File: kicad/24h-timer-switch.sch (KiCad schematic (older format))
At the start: 13 parts, among them J1 Barrel_Jack, J2 Screw_Terminal_01x02, Q1 AO4620, SW1 SW_SPST, U1 AMS1117-5.0, U2 ATtiny85-20PU

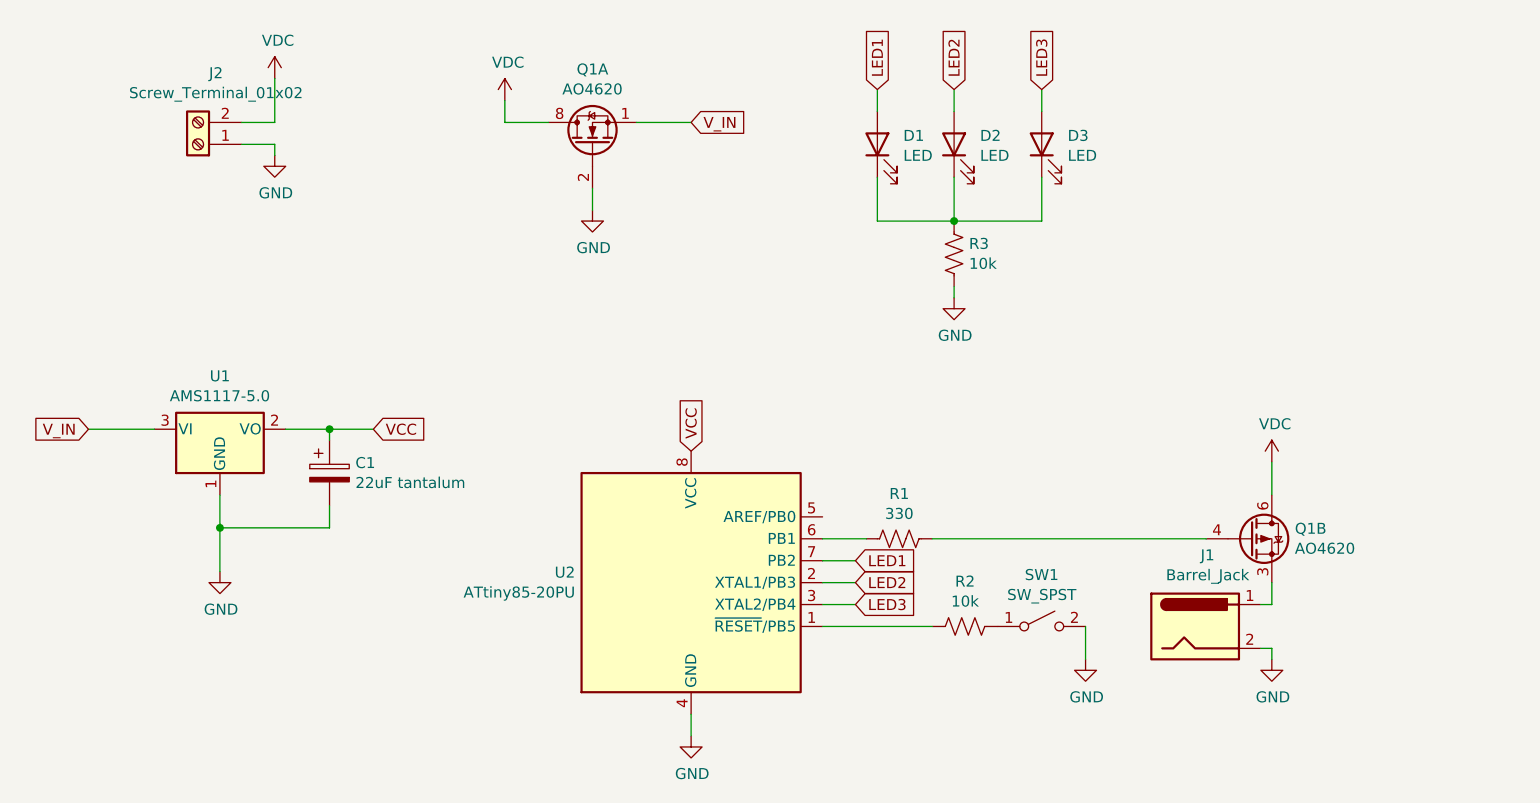
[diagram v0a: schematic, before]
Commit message: add jumper selector
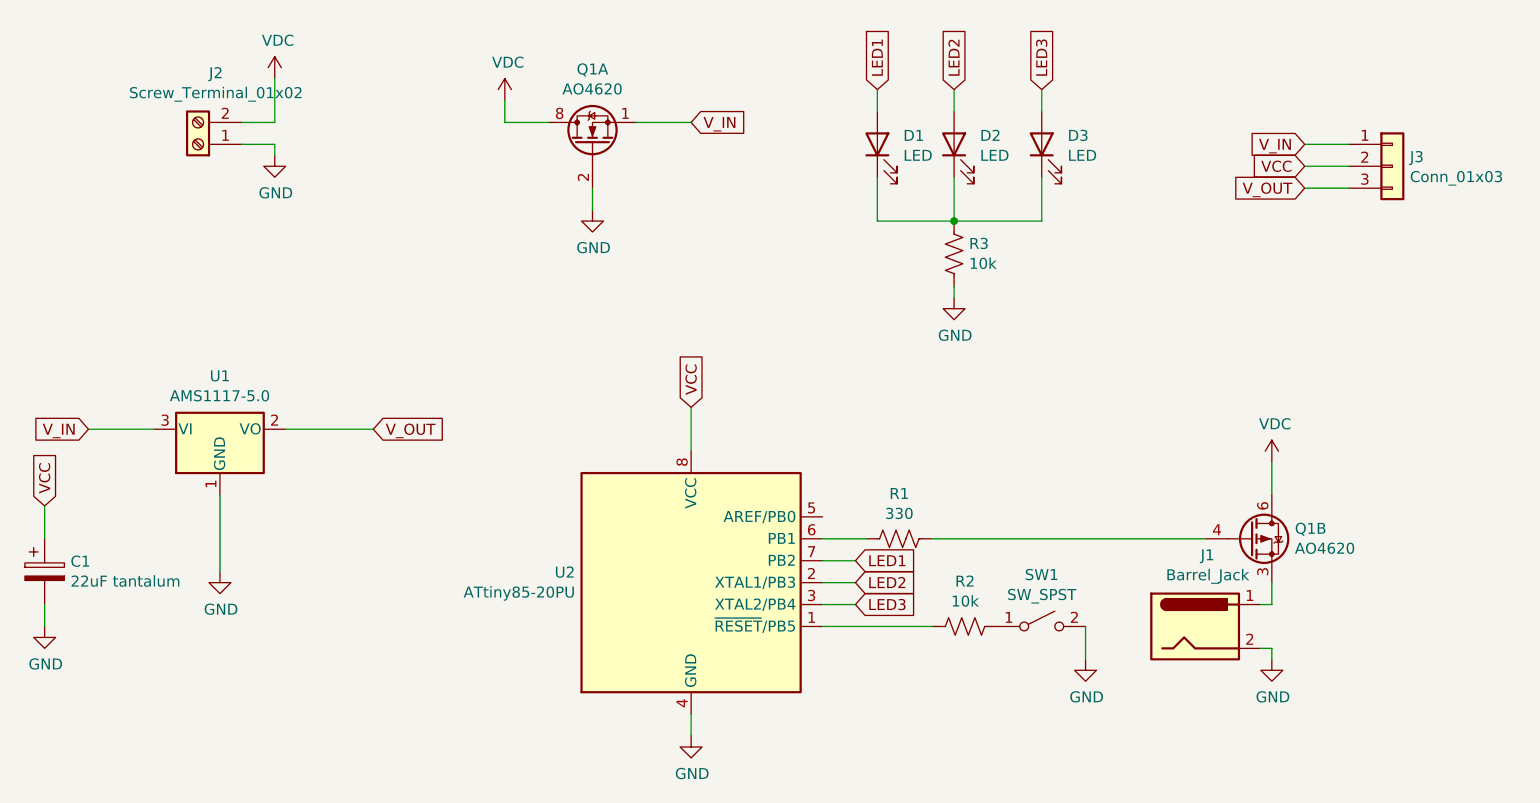
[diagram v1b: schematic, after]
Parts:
- added J3: Conn_01x03, Connector_PinSocket_2.54mm:PinSocket_1x03_P2.54mm_Vertical, symbol Connector_Generic:Conn_01x03
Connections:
- net VCC: now also J3.2 (Pin_2); no longer U1.2 (VO)
- net V_IN: now also J3.1 (Pin_1)
- new net V_OUT: J3.3 (Pin_3), U1.2 (VO)
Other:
- moved on the sheet: C1
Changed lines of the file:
@@
 	1    0    0    -1
 $EndComp
-Wire Wire Line
-	2200 2950 2200 3100
 $Comp
 L Device:CP C1
 U 1 1 61A472D0
-P 2700 2850
-F 0 "C1" H 2818 2896 50  0000 L CNN
-F 1 "22uF tantalum" H 2818 2805 50  0000 L CNN
-F 2 "Capacitor_THT:CP_Radial_D5.0mm_P2.50mm" H 2738 2700 50  0001 C CNN
-F 3 "~" H 2700 2850 50  0001 C CNN
-	1    2700 2850
-	1    0    0    -1
-$EndComp
-Wire Wire Line
-	2500 2650 2700 2650
-Wire Wire Line
-	2700 2650 2700 2700
-Wire Wire Line
-	2700 3000 2700 3100
-Wire Wire Line
-	2700 3100 2200 3100
-Wire Wire Line
-	2200 3100 2200 3300
-Connection ~ 2200 3100
+P 1400 3300
+F 0 "C1" H 1518 3346 50  0000 L CNN
+F 1 "22uF tantalum" H 1518 3255 50  0000 L CNN
+F 2 "Capacitor_THT:CP_Radial_D5.0mm_P2.50mm" H 1438 3150 50  0001 C CNN
+F 3 "~" H 1400 3300 50  0001 C CNN
+	1    1400 3300
+	1    0    0    -1
+$EndComp
 $Comp
 L power:VDC #PWR02
@@
 	1    0    0    -1
 $EndComp
-Wire Wire Line
-	2700 2650 2900 2650
-Connection ~ 2700 2650
 Text GLabel 2900 2650 2    50   Input ~ 0
-VCC
-Text GLabel 4350 2750 1    50   Input ~ 0
-VCC
+V_OUT
+Text GLabel 7150 1550 0    50   Input ~ 0
+V_OUT
 $Comp
 L Device:R_US R1
@@
 Wire Wire Line
 	7000 3650 6950 3650
+$Comp
+L Connector_Generic:Conn_01x03 J3
+U 1 1 61A4A1CB
+P 7550 1450
+F 0 "J3" H 7630 1492 50  0000 L CNN
+F 1 "Conn_01x03" H 7630 1401 50  0000 L CNN
+F 2 "Connector_PinSocket_2.54mm:PinSocket_1x03_P2.54mm_Vertical" H 7550 1450 50  0001 C CNN
+F 3 "~" H 7550 1450 50  0001 C CNN
+	1    7550 1450
+	1    0    0    -1
+$EndComp
+Wire Wire Line
+	7150 1550 7350 1550
+Text GLabel 7150 1350 0    50   Input ~ 0
+V_IN
+Wire Wire Line
+	7150 1350 7350 1350
+Text GLabel 4350 2550 1    50   Input ~ 0
+VCC
+Wire Wire Line
+	4350 2550 4350 2750
+Text GLabel 7150 1450 0    50   Input ~ 0
+VCC
+Wire Wire Line
+	7150 1450 7350 1450
+Wire Wire Line
+	2200 2950 2200 3300
+Wire Wire Line
+	2900 2650 2500 2650
+$Comp
+L power:GND #PWR?
+U 1 1 61A6F596
+P 1400 3550
+F 0 "#PWR?" H 1400 3300 50  0001 C CNN
+F 1 "GND" H 1405 3377 50  0000 C CNN
+F 2 "" H 1400 3550 50  0001 C CNN
+F 3 "" H 1400 3550 50  0001 C CNN
+	1    1400 3550
+	1    0    0    -1
+$EndComp
+Wire Wire Line
+	1400 3450 1400 3550
+Text GLabel 1400 3000 1    50   Input ~ 0
+VCC
+Wire Wire Line
+	1400 3000 1400 3150
 $EndSCHEMATC
